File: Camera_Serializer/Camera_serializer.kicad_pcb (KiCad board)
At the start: 2 copper layers, 2 parts, among them J1 7-2287906-0

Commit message: Finishe schematic
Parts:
- added C14: 13pF, Capacitor_SMD:C_0402_1005Metric, F.Cu at (151.5, 72.4)
- added C15: 13pF, Capacitor_SMD:C_0402_1005Metric, F.Cu at (151.5, 74.4)
- added C19: 0.1uF, Capacitor_SMD:C_0402_1005Metric_Pad0.74x0.62mm_HandSolder, F.Cu at (134.4, 67.3)
- added C20: 10uF, Capacitor_SMD:C_0805_2012Metric_Pad1.18x1.45mm_HandSolder, F.Cu at (138.5, 67.9)
- added C21: 3.3nF, Capacitor_SMD:C_0402_1005Metric_Pad0.74x0.62mm_HandSolder, F.Cu at (134.4, 69.3)
- added C22: 22uF, Capacitor_SMD:C_0603_1608Metric_Pad1.08x0.95mm_HandSolder, F.Cu at (124.7, 79.0)
- added C23: 22uF, Capacitor_SMD:C_0603_1608Metric_Pad1.08x0.95mm_HandSolder, F.Cu at (124.7, 81.5)
- added C24: 10uF, Capacitor_SMD:C_0805_2012Metric_Pad1.18x1.45mm_HandSolder, F.Cu at (138.5, 70.9)
- added C25: 0.1uF, Capacitor_SMD:C_0402_1005Metric_Pad0.74x0.62mm_HandSolder, F.Cu at (134.4, 71.3)
- added C26: 3.3nF, Capacitor_SMD:C_0402_1005Metric_Pad0.74x0.62mm_HandSolder, F.Cu at (134.4, 73.3)
- added D1: ~, Diode_SMD:D_0402_1005Metric, F.Cu at (146.1, 104.7)
- added D2: GREEN, LED_SMD:LED_0603_1608Metric_Pad1.05x0.95mm_HandSolder, F.Cu at (134.0, 79.0)
- added D3: GREEN, LED_SMD:LED_0603_1608Metric_Pad1.05x0.95mm_HandSolder, F.Cu at (134.0, 81.6)
- added D4: GREEN, LED_SMD:LED_0603_1608Metric_Pad1.05x0.95mm_HandSolder, F.Cu at (134.0, 84.2)
- added J2: F32Q-1A7H1-11022, CameraServer_Footprints:F32Q-1A7H1-11022, F.Cu at (128.4, 96.8)
- added L4: 2.2uH, CameraServer_Footprints:IFSC1515AHER2R2M01, F.Cu at (126.4, 69.2)
- added L5: 2.2uH, CameraServer_Footprints:IFSC1515AHER2R2M01, F.Cu at (126.4, 74.9)
- added Q1: BSS138, Package_TO_SOT_SMD:SOT-23, F.Cu at (129.3, 80.1)
- added Q2: BSS138, Package_TO_SOT_SMD:SOT-23, F.Cu at (129.3, 84.7)
- added R1: 49.9, Resistor_SMD:R_0402_1005Metric, F.Cu at (148.6, 72.5)
- added R14: 100, Resistor_SMD:R_0402_1005Metric_Pad0.72x0.64mm_HandSolder, F.Cu at (120.1, 102.1)
- added R15: 100, Resistor_SMD:R_0402_1005Metric_Pad0.72x0.64mm_HandSolder, F.Cu at (120.1, 104.1)
- added R16: 4k7, Resistor_SMD:R_0402_1005Metric_Pad0.72x0.64mm_HandSolder, F.Cu at (120.1, 106.0)
- added R17: 4k7, Resistor_SMD:R_0402_1005Metric_Pad0.72x0.64mm_HandSolder, F.Cu at (120.1, 108.0)
- added R18: 100k, Resistor_SMD:R_0402_1005Metric_Pad0.72x0.64mm_HandSolder, F.Cu at (131.2, 67.4)
- added R19: 100k, Resistor_SMD:R_0402_1005Metric_Pad0.72x0.64mm_HandSolder, F.Cu at (131.2, 69.3)
- added R20: 330, Resistor_SMD:R_0603_1608Metric_Pad0.98x0.95mm_HandSolder, F.Cu at (124.7, 84.0)
- added R21: 820, Resistor_SMD:R_0603_1608Metric_Pad0.98x0.95mm_HandSolder, F.Cu at (124.7, 86.5)
- added R22: 100k, Resistor_SMD:R_0402_1005Metric_Pad0.72x0.64mm_HandSolder, F.Cu at (131.2, 71.3)
- added R23: 100k, Resistor_SMD:R_0402_1005Metric_Pad0.72x0.64mm_HandSolder, F.Cu at (131.2, 73.3)
- added R24: 820, Resistor_SMD:R_0603_1608Metric_Pad0.98x0.95mm_HandSolder, F.Cu at (124.7, 89.0)
- added R3: 402, Resistor_SMD:R_0402_1005Metric, F.Cu at (148.6, 74.4)
- added R5: 10k, Resistor_SMD:R_0402_1005Metric, F.Cu at (148.6, 76.4)
- added TP1: TestPoint, TestPoint:TestPoint_Pad_D1.0mm, F.Cu at (145.1, 68.4)
- added TP2: TestPoint, TestPoint:TestPoint_Pad_D1.0mm, F.Cu at (145.1, 72.4)
- added TP3: TestPoint, TestPoint:TestPoint_Pad_D1.0mm, F.Cu at (145.1, 76.5)
- added TP4: TestPoint, TestPoint:TestPoint_Pad_D1.0mm, F.Cu at (142.4, 105.8)
- added TP5: TestPoint, TestPoint:TestPoint_Pad_D1.0mm, F.Cu at (120.5, 68.4)
- added TP6: TestPoint, TestPoint:TestPoint_Pad_D1.0mm, F.Cu at (120.5, 72.4)
- added TP7: TestPoint, TestPoint:TestPoint_Pad_D1.0mm, F.Cu at (120.5, 76.5)
- added TP8: TestPoint, TestPoint:TestPoint_Pad_D1.0mm, F.Cu at (120.5, 80.5)
- added U2: PUSB3FR4Z, CameraServer_Footprints:PUSB3FR4Z, F.Cu at (123.8, 103.2)
- added U3: TPS62133RGTR, CameraServer_Footprints:TPS62133RGTR, F.Cu at (138.8, 74.7)
- added U4: TPS62131RGTT, Snapeda:RGT0016C, F.Cu at (138.5, 80.0)
- added U5: ~, CameraServer_Footprints:NCP114ASN120T1G, F.Cu at (134.8, 87.7)
- added U6: MIC5528-3.3YMT-TR, Snapeda:TDFN6_1P2X1P2_MCH, F.Cu at (138.1, 83.6)
- added Y1: ~, CameraServer_Footprints:EB2532YA08-25.000M_TR, F.Cu at (150.2, 68.9)
- J1: value 7-2287906-0 -> ~; footprint 7-2287906-0:722879060 -> CameraServer_Footprints:7-2287906-0
- U1: footprint Package_DFN_QFN:TQFN-32-1EP_5x5mm_P0.5mm_EP3.1x3.1mm -> CameraServer_Footprints:QFN50P500X500X80-33N
- moved J1 57.4 mm to (159.7, 95.0)
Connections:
- J1 pad 1: unconnected-(J1-Pad1) -> /GMSL_Connector/SIOP_COAX
- J1 pad 2: unconnected-(J1-Pad2) -> GND
- J1 pad 3: unconnected-(J1-Pad3) -> (no net)
- J1 pad 4: unconnected-(J1-Pad4) -> (no net)
- J1 pad 5: unconnected-(J1-Pad5) -> (no net)
- U1 pad 1: unconnected-(U1-PWDNB-Pad1) -> /serializer/PWDN
- U1 pad 10: unconnected-(U1-XRES-Pad10) -> /serializer/XRES
- U1 pad 12: unconnected-(U1-SIOP-Pad12) -> Net-(U1-SIOP)
- U1 pad 17: unconnected-(U1-MFP3-Pad17) -> /serializer/GPIO3
- U1 pad 18: unconnected-(U1-MFP4-Pad18) -> /serializer/GPIO4
- U1 pad 19: /serializer/CSI.D2_P -> /csi/CSI.D2_P
- U1 pad 2: unconnected-(U1-MFP0-Pad2) -> Net-(U1-MFP0)
- U1 pad 20: /serializer/CSI.D2_N -> /csi/CSI.D2_N
- U1 pad 21: unconnected-(U1-MFP5-Pad21) -> Net-(U1-MFP5)
- U1 pad 22: unconnected-(U1-MFP6-Pad22) -> Net-(U1-MFP6)
- U1 pad 23: /serializer/CSI.D3_P -> /csi/CSI.D3_P
- U1 pad 24: /serializer/CSI.D3_N -> /csi/CSI.D3_N
- U1 pad 25: /serializer/CSI.D0_P -> /csi/CSI.D0_P
- U1 pad 26: /serializer/CSI.D0_N -> /csi/CSI.D0_N
- U1 pad 27: /serializer/CSI.CK_P -> /csi/CSI.CK_P
- U1 pad 28: /serializer/CSI.CK_N -> /csi/CSI.CK_N
- U1 pad 29: /serializer/CSI.D1_P -> /csi/CSI.D1_P
- U1 pad 3: unconnected-(U1-MFP1-Pad3) -> /serializer/CFG0
- U1 pad 30: /serializer/CSI.D1_N -> /csi/CSI.D1_N
- U1 pad 31: unconnected-(U1-MFP7-Pad31) -> Net-(U1-MFP7)
- U1 pad 32: unconnected-(U1-MFP8-Pad32) -> Net-(U1-MFP8)
- U1 pad 33: (no net) -> GND
- U1 pad 4: unconnected-(U1-MFP2-Pad4) -> /serializer/CFG1
- U1 pad 5: unconnected-(U1-MFP9-Pad5) -> Net-(U1-MFP9)
- U1 pad 6: unconnected-(U1-MFP10-Pad6) -> Net-(U1-MFP10)
- U1 pad 7: unconnected-(U1-V_REF-Pad7) -> /serializer/VREF
- U1 pad 8: unconnected-(U1-X1-Pad8) -> /serializer/X1
- U1 pad 9: unconnected-(U1-X2-Pad9) -> /serializer/X2

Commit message: Layout started
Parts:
- added C1: 10n, Capacitor_SMD:C_0402_1005Metric_Pad0.74x0.62mm_HandSolder, F.Cu at (143.2, 29.5)
- added C10: 100n, Capacitor_SMD:C_0402_1005Metric_Pad0.74x0.62mm_HandSolder, F.Cu at (146.4, 37.4)
- added C11: 10u, Capacitor_SMD:C_0402_1005Metric_Pad0.74x0.62mm_HandSolder, F.Cu at (149.6, 29.5)
- added C12: 100n, Capacitor_SMD:C_0402_1005Metric_Pad0.74x0.62mm_HandSolder, F.Cu at (145.9, 51.4)
- added C13: 100n, Capacitor_SMD:C_0402_1005Metric_Pad0.74x0.62mm_HandSolder, F.Cu at (149.6, 31.5)
- added C16: 10n, Capacitor_SMD:C_0402_1005Metric_Pad0.74x0.62mm_HandSolder, F.Cu at (149.6, 33.5)
- added C17: 100n, Capacitor_SMD:C_0402_1005Metric_Pad0.74x0.62mm_HandSolder, F.Cu at (146.3, 92.5)
- added C18: 10n, Capacitor_SMD:C_0402_1005Metric_Pad0.74x0.62mm_HandSolder, F.Cu at (147.1, 73.7)
- added C2: 100n, Capacitor_SMD:C_0402_1005Metric_Pad0.74x0.62mm_HandSolder, F.Cu at (143.2, 31.5)
- added C27: 1uF, Capacitor_SMD:C_0402_1005Metric_Pad0.74x0.62mm_HandSolder, F.Cu at (151.7, 51.4)
- added C28: 1uF, Capacitor_SMD:C_0402_1005Metric_Pad0.74x0.62mm_HandSolder, F.Cu at (151.7, 53.3)
- added C29: 1uF, Capacitor_SMD:C_0402_1005Metric_Pad0.74x0.62mm_HandSolder, F.Cu at (151.7, 55.3)
- added C3: 10u, Capacitor_SMD:C_0402_1005Metric_Pad0.74x0.62mm_HandSolder, F.Cu at (143.2, 33.5)
- added C30: 1uF, Capacitor_SMD:C_0402_1005Metric_Pad0.74x0.62mm_HandSolder, F.Cu at (151.7, 57.3)
- added C4: 10n, Capacitor_SMD:C_0402_1005Metric_Pad0.74x0.62mm_HandSolder, F.Cu at (143.2, 35.4)
- added C5: 100n, Capacitor_SMD:C_0402_1005Metric_Pad0.74x0.62mm_HandSolder, F.Cu at (143.2, 37.4)
- added C6: 10u, Capacitor_SMD:C_0402_1005Metric_Pad0.74x0.62mm_HandSolder, F.Cu at (146.4, 29.5)
- added C7: 10n, Capacitor_SMD:C_0402_1005Metric_Pad0.74x0.62mm_HandSolder, F.Cu at (146.4, 31.5)
- added C8: 100n, Capacitor_SMD:C_0402_1005Metric_Pad0.74x0.62mm_HandSolder, F.Cu at (146.4, 33.5)
- added C9: 10u, Capacitor_SMD:C_0402_1005Metric_Pad0.74x0.62mm_HandSolder, F.Cu at (146.4, 35.4)
- added H1: MountingHole_Pad, MountingHole:MountingHole_2.5mm_Pad, F.Cu at (135.9, 80.5)
- added H2: MountingHole_Pad, MountingHole:MountingHole_2.5mm_Pad, F.Cu at (166.4, 80.5)
- added H3: MountingHole_Pad, MountingHole:MountingHole_2.5mm_Pad, F.Cu at (166.4, 111.0)
- added H4: MountingHole_Pad, MountingHole:MountingHole_2.5mm_Pad, F.Cu at (135.9, 111.0)
- added L1: 560n, CameraServer_Footprints:PFL1609-561MEW, F.Cu at (156.5, 87.9)
- added L2: 6u8, CameraServer_Footprints:1812PS-682JRC, F.Cu at (160.0, 80.3)
- added L3: 22u, CameraServer_Footprints:SRN3015C-220M, F.Cu at (154.7, 78.5)
- added R10: 0R, Resistor_SMD:R_0402_1005Metric_Pad0.72x0.64mm_HandSolder, F.Cu at (140.0, 41.5)
- added R11: 0R, Resistor_SMD:R_0402_1005Metric_Pad0.72x0.64mm_HandSolder, F.Cu at (140.0, 43.5)
- added R12: 5k, Resistor_SMD:R_0402_1005Metric_Pad0.72x0.64mm_HandSolder, F.Cu at (146.0, 58.5)
- added R13: 5k, Resistor_SMD:R_0402_1005Metric_Pad0.72x0.64mm_HandSolder, F.Cu at (160.0, 72.3)
- added R2: 0R, Resistor_SMD:R_0402_1005Metric_Pad0.72x0.64mm_HandSolder, F.Cu at (140.0, 29.5)
- added R4: ~, Resistor_SMD:R_0402_1005Metric_Pad0.72x0.64mm_HandSolder, F.Cu at (140.0, 31.5)
- added R6: 10k, Resistor_SMD:R_0402_1005Metric_Pad0.72x0.64mm_HandSolder, F.Cu at (140.0, 33.5)
- added R7: ~, Resistor_SMD:R_0402_1005Metric_Pad0.72x0.64mm_HandSolder, F.Cu at (140.0, 35.5)
- added R8: 10K, Resistor_SMD:R_0402_1005Metric_Pad0.72x0.64mm_HandSolder, F.Cu at (140.0, 37.5)
- added R9: 0R, Resistor_SMD:R_0402_1005Metric_Pad0.72x0.64mm_HandSolder, F.Cu at (140.0, 39.5)
- U4: footprint Snapeda:RGT0016C -> CameraServer_Footprints:TPS62133RGTR
- moved L5 67.4 mm to (193.5, 68.1)
- moved U1 65.1 mm to (146.1, 97.9), turned to 180 degrees
- moved U5 37.0 mm to (97.9, 89.3)
- moved C24 37.0 mm to (101.5, 71.3)
- moved U6 37.0 mm to (101.2, 84.1)
- moved Q1 37.0 mm to (92.4, 80.5)
- moved Q2 37.0 mm to (92.4, 85.2)
- moved R14 37.0 mm to (83.2, 102.5)
- moved R19 37.0 mm to (94.3, 69.8)
- moved R22 37.0 mm to (94.3, 71.8)
- moved R23 37.0 mm to (94.3, 73.8)
- moved TP5 37.0 mm to (83.6, 68.8)
- moved TP6 37.0 mm to (83.6, 72.9)
- moved TP7 37.0 mm to (83.6, 76.9)
- moved TP8 37.0 mm to (83.6, 81.0)
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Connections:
- J2 pad SH1: (no net) -> GND
- J2 pad SH2: (no net) -> GND
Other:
- board outline added: 38.1 x 38.1 mm
- copper layers 2 -> 4

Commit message: All components placed in correct positions
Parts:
- removed TP6: TestPoint, TestPoint:TestPoint_Pad_D1.0mm
- added D5: GREEN, LED_SMD:LED_0603_1608Metric_Pad1.05x0.95mm_HandSolder, F.Cu at (167.4, 106.4)
- added R25: 820, Resistor_SMD:R_0603_1608Metric_Pad0.98x0.95mm_HandSolder, F.Cu at (164.8, 105.4)
- C20: footprint Capacitor_SMD:C_0805_2012Metric_Pad1.18x1.45mm_HandSolder -> Capacitor_SMD:C_0805_2012Metric
- L4, L5: footprint CameraServer_Footprints:IFSC1515AHER2R2M01 -> Inductor_SMD:L_1008_2520Metric
- U5: value ~ -> TPS73601DBVR; footprint CameraServer_Footprints:NCP114ASN120T1G -> CameraServer_Footprints:TPS73601DBVR
- moved R20 80.0 mm to (165.6, 102.9), turned to 90 degrees
- moved R24 78.5 mm to (165.6, 99.3), turned to 90 degrees
- moved R21 78.3 mm to (165.6, 95.8), turned to 90 degrees
- moved D2 74.1 mm to (167.4, 102.9), turned to 90 degrees
- moved R2 73.4 mm to (143.8, 102.9), turned to -135 degrees
- moved R4 72.9 mm to (148.8, 103.9), turned to -45 degrees
- moved R14 72.0 mm to (155.2, 102.6), turned to 90 degrees
- moved Q1 71.9 mm to (162.6, 95.8)
- moved D4 71.9 mm to (167.4, 99.3), turned to 90 degrees
- moved D3 71.7 mm to (167.4, 95.8), turned to 90 degrees
- moved Q2 71.6 mm to (162.6, 99.3)
- moved R23 70.5 mm to (160.0, 99.3), turned to -90 degrees
- moved R22 70.0 mm to (160.0, 95.8), turned to -90 degrees
- moved R7 68.6 mm to (149.9, 103.4), turned to -45 degrees
- moved R6 68.6 mm to (148.1, 101.6), turned to 135 degrees
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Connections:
- C27 pad 1: +5V -> +1V8
- U5 pad 1: +5V -> +1V8
- U5 pad 3: +5V -> +1V8
- U5 pad 4: unconnected-(U5-NC-Pad4) -> +1V8
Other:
- board text added: "1.2V"
- board text added: "1.8V"
- board text added: "3.3V"
- board text added: "5V"

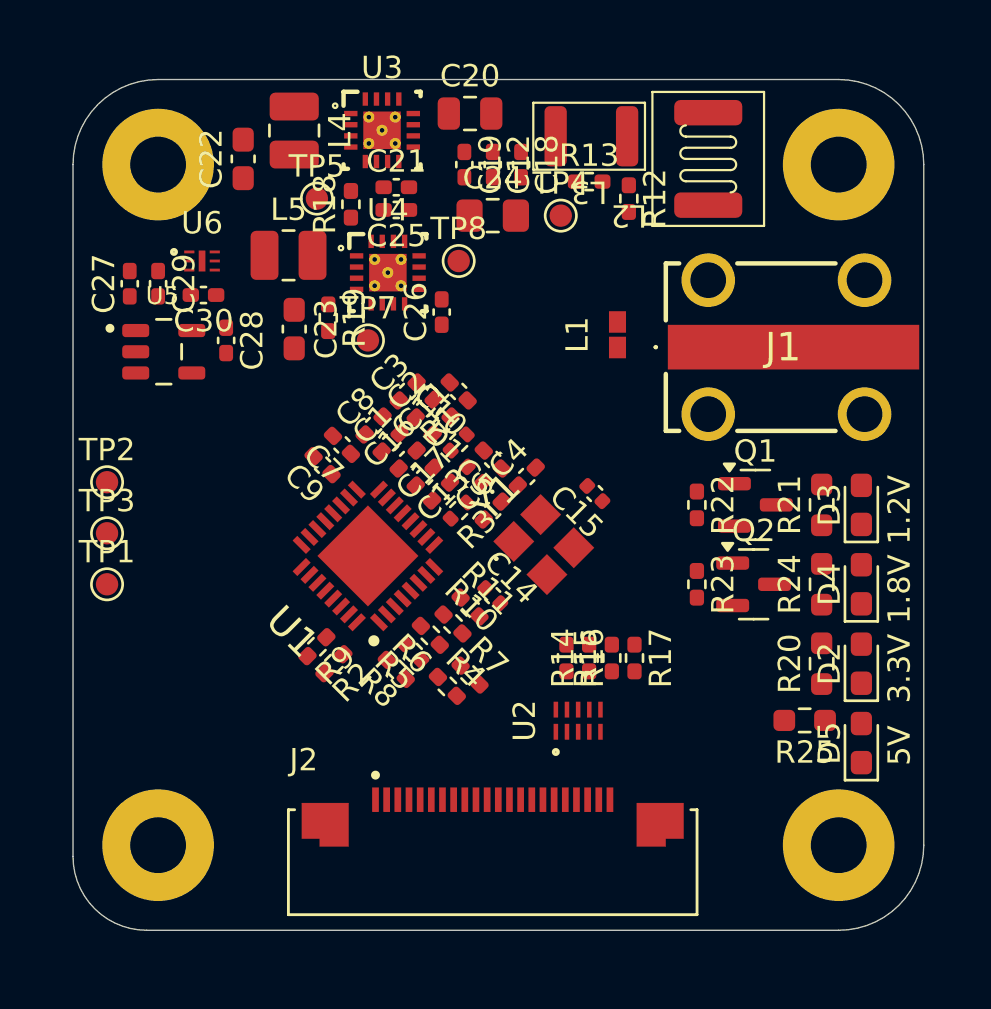
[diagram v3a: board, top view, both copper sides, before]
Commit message: Routed most traces except CSI lines
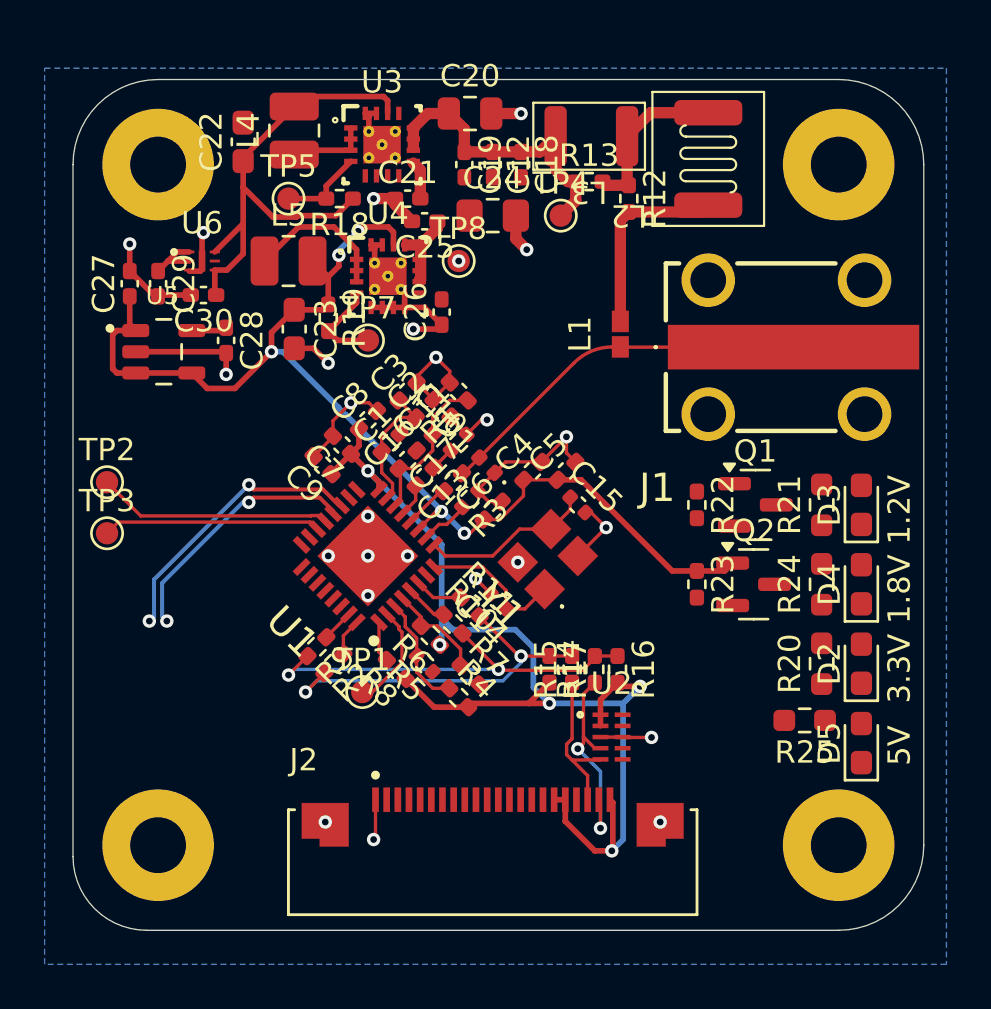
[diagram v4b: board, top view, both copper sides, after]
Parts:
- moved TP1 12.4 mm to (145.0, 104.1)
- moved R17 3.84 mm to (153.4, 103.1)
- moved C5 3.34 mm to (154.2, 94.2), turned to 45 degrees
- moved R16 2.34 mm to (156.5, 103.1)
- moved R15 1.85 mm to (154.4, 103.1)
- moved U2 1.67 mm to (156.2, 106.2), turned to 0 degrees
- moved C25 1.37 mm to (147.8, 83.1)
- moved TP5 1.27 mm to (141.7, 82.0)
- moved C15 0.92 mm to (154.7, 95.8), turned to -45 degrees
- moved C22 0.76 mm to (139.7, 79.5)
- moved R4 0.72 mm to (149.4, 104.4)
- moved R5 0.72 mm to (147.8, 102.9)
- moved C21 0.72 mm to (147.1, 82.0)
- moved R3 0.72 mm to (149.9, 95.5)
- moved C17 0.68 mm to (149.1, 94.7)
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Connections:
- U3 pad 18: (no net) -> GND
- U3 pad 19: (no net) -> GND
- U3 pad 20: (no net) -> GND
- U3 pad 21: (no net) -> GND
- U3 pad 22: (no net) -> GND
- U4 pad 18: (no net) -> GND
- U4 pad 19: (no net) -> GND
- U4 pad 20: (no net) -> GND
- U4 pad 21: (no net) -> GND
- U4 pad 22: (no net) -> GND
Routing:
- net GND: track 0.00 -> 54.7 mm, vias 0 -> 25
- net +3V3: track 0.00 -> 53.3 mm, vias 0 -> 5
- net +1V8: track 0.00 -> 52.2 mm, vias 0 -> 5
- net +5V: track 0.00 -> 22.9 mm
- net /GMSL_Connector/SIOP_COAX: track 0.00 -> 22.6 mm
- net /csi/I2C.SDA: track 0.00 -> 18.6 mm, vias 0 -> 2
- net +12V: track 0.00 -> 17.2 mm
- net /csi/I2C.SCL: track 0.00 -> 16.6 mm, vias 0 -> 2
- net /csi/CSI.D2_P: track 0.00 -> 12.5 mm, vias 0 -> 2
- net /csi/CSI.D2_N: track 0.00 -> 11.4 mm, vias 0 -> 2
- net Net-(U1-MFP5): track 0.00 -> 10.5 mm
- net Net-(U1-MFP6): track 0.00 -> 9.76 mm
- net /csi/CAM_SDA: track 0.00 -> 9.53 mm, vias 0 -> 2
- net Net-(L1-Pad2): track 0.00 -> 8.74 mm
- net /serializer/X2: track 0.00 -> 7.98 mm
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- added copper zone on B.Cu, net GND
- added copper zone on In1.Cu, net GND
- added copper zone on In2.Cu, net GND

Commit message: Finished routing
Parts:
- 1V8 PG: renamed from TP7
- 5V PG: renamed from TP5
- moved GND 20.8 mm to (134.4, 99.3)
- moved MFP5 0.76 mm to (134.4, 94.7)
- moved MFP6 0.76 mm to (134.4, 97.0)
- moved 1V8 PG 0.51 mm to (145.8, 88.4)
- turned C1 to -135 degrees
- renumbered TP8 to GND, TP2 to MFP5, TP3 to MFP6
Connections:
- C21 pad 1: GND -> Net-(U3-SS_TR)
- C21 pad 2: Net-(U3-SS_TR) -> GND
- J1 pad 3: (no net) -> GND
- J1 pad 4: (no net) -> GND
- J1 pad 5: (no net) -> GND
- U3 pad 18: GND -> (no net)
- U3 pad 19: GND -> (no net)
- U3 pad 20: GND -> (no net)
- U3 pad 21: GND -> (no net)
- U3 pad 22: GND -> (no net)
- U4 pad 18: GND -> (no net)
- U4 pad 19: GND -> (no net)
- U4 pad 20: GND -> (no net)
- U4 pad 21: GND -> (no net)
- U4 pad 22: GND -> (no net)
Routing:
- net +5V: track 22.9 -> 72.0 mm, vias 0 -> 2
- net GND: track 54.7 -> 102.3 mm, vias 25 -> 38
- net /csi/CSI.D3_P: track 0.00 -> 32.5 mm, vias 0 -> 2
- net /csi/CSI.D3_N: track 0.00 -> 30.4 mm, vias 0 -> 2
- net /csi/CSI.D2_N: track 11.4 -> 38.5 mm
- net +1V2: track 7.62 -> 34.5 mm, vias 0 -> 3
- net +3V3: track 53.3 -> 79.2 mm, vias 5 -> 7
- net /csi/CSI.D2_P: track 12.5 -> 38.0 mm
- net /csi/CSI.CK_P: track 0.00 -> 22.3 mm, vias 0 -> 2
- net /csi/CSI.D1_P: track 0.00 -> 21.5 mm, vias 0 -> 2
- net /csi/CSI.CK_N: track 0.00 -> 21.0 mm, vias 0 -> 2
- net /csi/CSI.D1_N: track 0.00 -> 20.6 mm, vias 0 -> 2
- net /csi/CSI.D0_P: track 0.00 -> 20.1 mm, vias 0 -> 2
- net /csi/CSI.D0_N: track 0.00 -> 18.5 mm, vias 0 -> 2
- net +12V: track 17.2 -> 23.6 mm
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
